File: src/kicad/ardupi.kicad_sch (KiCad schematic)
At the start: 60 parts, among them J1 Conn_01x02, J10 Conn_01x04, J11 TSW-108-08-L-T-RA, J2 Conn_01x10, J3 Conn_01x05, J4 Conn_01x04, J5 GPIO_CONNECTOR, J6 Conn_01x05, J7 Conn_01x06, J8 Conn_01x04, J9 Conn_01x02, U1 CAT24C256, U2 ULN2803ADW, U3 PCA9685BS, U4 ADS1115IRUGR, U5 MPU-9250, U6 BMP280

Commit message: fix layout
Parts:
- removed BT1: Battery, symbol Device:Battery
- removed C1: 100n, symbol Device:C_Small
- removed J1: Conn_01x02, Connector_JST:JST_EH_B2B-EH-A_1x02_P2.50mm_Vertical, symbol ardupi:Conn_01x02
- removed J5: GPIO_CONNECTOR, lib:PinSocket_2x20_P2.54mm_Vertical_Centered_Anchor, symbol Connector_Generic:Conn_02x20_Odd_Even
- removed JP1: ID_WP, symbol Jumper:SolderJumper_2_Open
- removed R1, R2: 3.9k, symbol Device:R_Small
- added C9: 100n, symbol Device:C_Small
- added J1: GPIO, Connector_PinSocket_2.54mm:PinSocket_2x20_P2.54mm_Vertical, symbol Connector_Generic:Conn_02x20_Odd_Even
- added JP2: ID_WP, symbol Jumper:SolderJumper_2_Open
- added R21, R22: 3.9k, symbol Device:R_Small
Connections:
- net +3V3: now also U1.8 (VCC), C9.2, J1.1 (Pin_1), J1.17 (Pin_17), JP2.2 (B), R21.2, R22.1
- net +5V: now also J1.2 (Pin_2), J1.4 (Pin_4)
- net BUZZER: now also J1.32 (Pin_32)
- net GND: now also U1.4 (VSS), C9.1, J1.14 (Pin_14), J1.20 (Pin_20), J1.25 (Pin_25), J1.30 (Pin_30), J1.34 (Pin_34), J1.39 (Pin_39), J1.6 (Pin_6), J1.9 (Pin_9)
- net GPIO14_TXD0: now also J1.8 (Pin_8)
- net GPIO15_RXD0: now also J1.10 (Pin_10)
- net GPIO18_GEN1: now also J1.12 (Pin_12)
- net GPIO23: now also J1.16 (Pin_16)
- net GPIO24: now also J1.18 (Pin_18)
- net GPIO25_GEN6: now also J1.22 (Pin_22)
- net ID_SCL: now also U1.6 (SCL), U1.7 (WP), J1.28 (Pin_28), JP2.1 (A), R22.2
- net ID_SDA: now also U1.5 (SDA), J1.27 (Pin_27), R21.1
- net LED1: now also J1.13 (Pin_13)
- net LED2: now also J1.15 (Pin_15)
- net LED3: now also J1.7 (Pin_7)
- net RC1: now also J1.29 (Pin_29)
- net RC2: now also J1.31 (Pin_31)
- net RC3: now also J1.33 (Pin_33)
- net RC4: now also J1.35 (Pin_35)
- net RC5: now also J1.37 (Pin_37)
- net RC6: now also J1.40 (Pin_40)
- net RC7: now also J1.38 (Pin_38)
- net RC8: now also J1.36 (Pin_36)
- net SCL1: now also J1.5 (Pin_5)
- net SDA1: now also J1.3 (Pin_3)
- net SPI_CE0_N: now also J1.24 (Pin_24)
- net SPI_CE1_N: now also J1.26 (Pin_26)
- net SPI_MISO: now also J1.21 (Pin_21)
- net SPI_MOSI: now also J1.19 (Pin_19)
- net SPI_SCLK: now also J1.23 (Pin_23)
- net SRVO_EN: now also J1.11 (Pin_11)
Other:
- title: ArduPi -> (none)
- moved on the sheet: C_PCA1, J11, R3, R4, R5, U1, U3

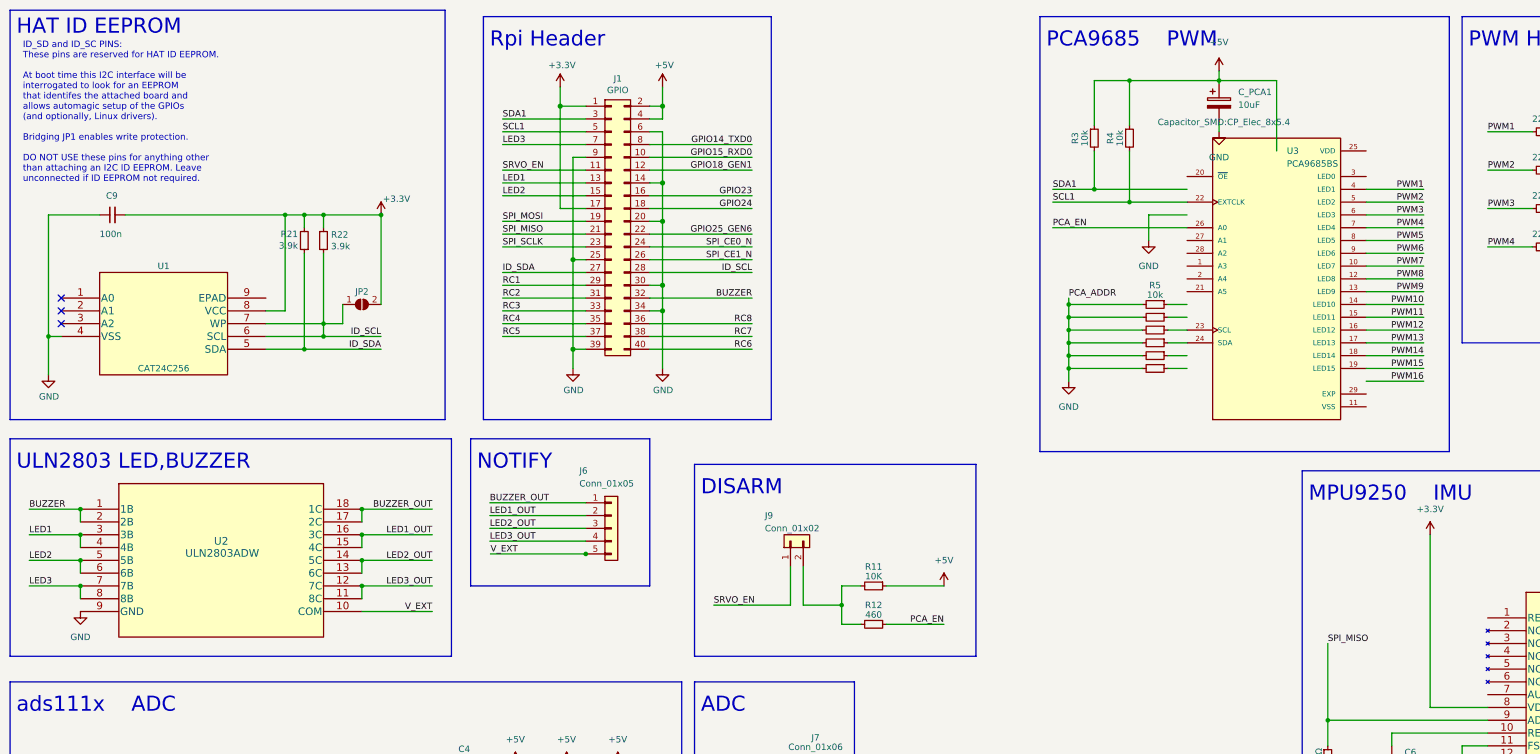
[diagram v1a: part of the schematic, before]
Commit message: replaced pca9685bs back to pca9685PW.
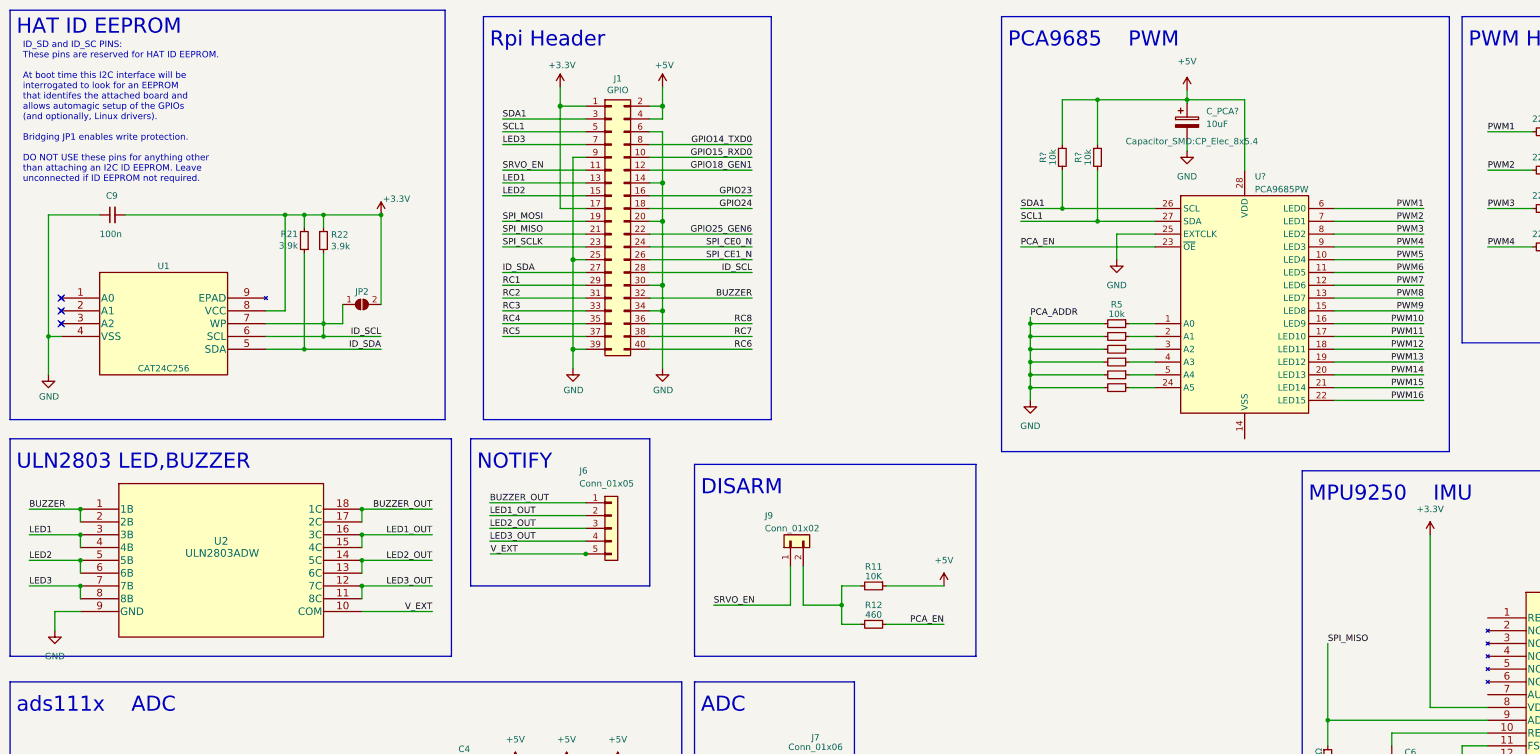
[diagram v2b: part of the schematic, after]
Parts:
- removed C_PCA1: 10uF, Capacitor_SMD:CP_Elec_8x5.4, symbol Device:C_Polarized
- removed R3, R4: 10k, Resistor_SMD:R_0402_1005Metric, symbol Device:R_Small
- removed U3: PCA9685BS, Ardupi:PCA9685BS_118, symbol ardupi:PCA9685BS,118
- added C_PCA?: 10uF, Capacitor_SMD:CP_Elec_8x5.4, symbol Device:C_Polarized
- added R? (x2): 10k, Resistor_SMD:R_0402_1005Metric, symbol Device:R_Small
- added U?: PCA9685PW, Package_SO:TSSOP-28_4.4x9.7mm_P0.65mm, symbol Driver_LED:PCA9685PW
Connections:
- net +5V: now also C_PCA?.1, R?.1, R?.1, U?.28 (VDD)
- net GND: now also C_PCA?.2, U?.25 (EXTCLK)
- net PCA_EN: now also U?.23 (~{OE})
- net PWM1: now also U?.6 (LED0)
- net PWM10: now also U?.16 (LED9)
- net PWM11: now also U?.17 (LED10)
- net PWM12: now also U?.18 (LED11)
- net PWM13: now also U?.19 (LED12)
- net PWM14: now also U?.20 (LED13)
- net PWM15: now also U?.21 (LED14)
- net PWM16: now also U?.22 (LED15)
- net PWM2: now also U?.7 (LED1)
- net PWM3: now also U?.8 (LED2)
- net PWM4: now also U?.9 (LED3)
- net PWM5: now also U?.10 (LED4)
- net PWM6: now also U?.11 (LED5)
- net PWM7: now also U?.12 (LED6)
- net PWM8: now also U?.13 (LED7)
- net PWM9: now also U?.15 (LED8)
- net SCL1: now also R?.2, U?.27 (SDA)
- net SDA1: now also R?.2, U?.26 (SCL)
- net at R7.1: now also U?.3 (A2)
- net at R6.1: now also U?.2 (A1)
- net at R8.1: now also U?.4 (A3)
- net at R5.1: now also U?.1 (A0)
- net at R10.1: now also U?.24 (A5)
- net at R9.1: now also U?.5 (A4)
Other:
- moved on the sheet: R5

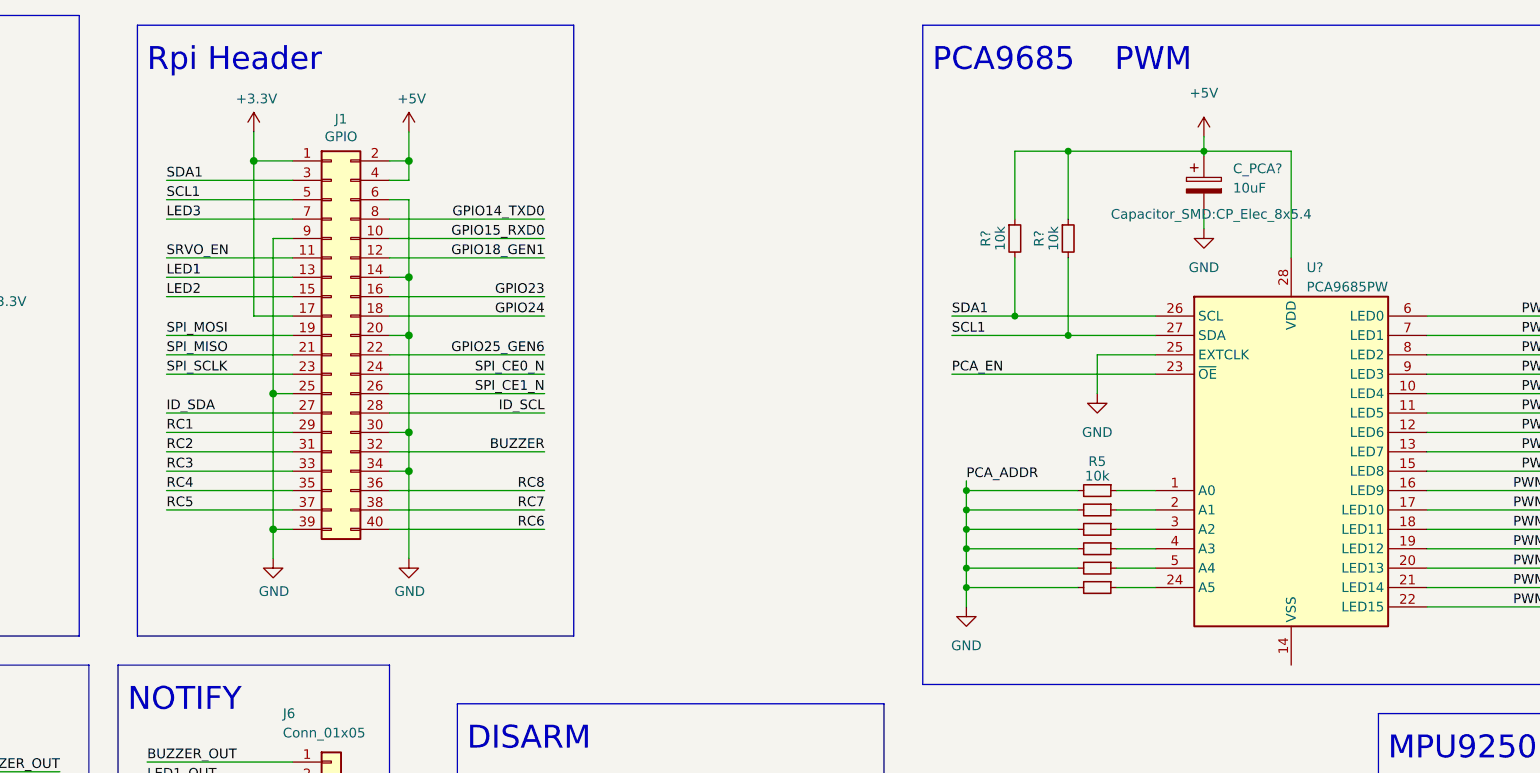
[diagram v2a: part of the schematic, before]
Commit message: pca9685bs -> pca9685PW
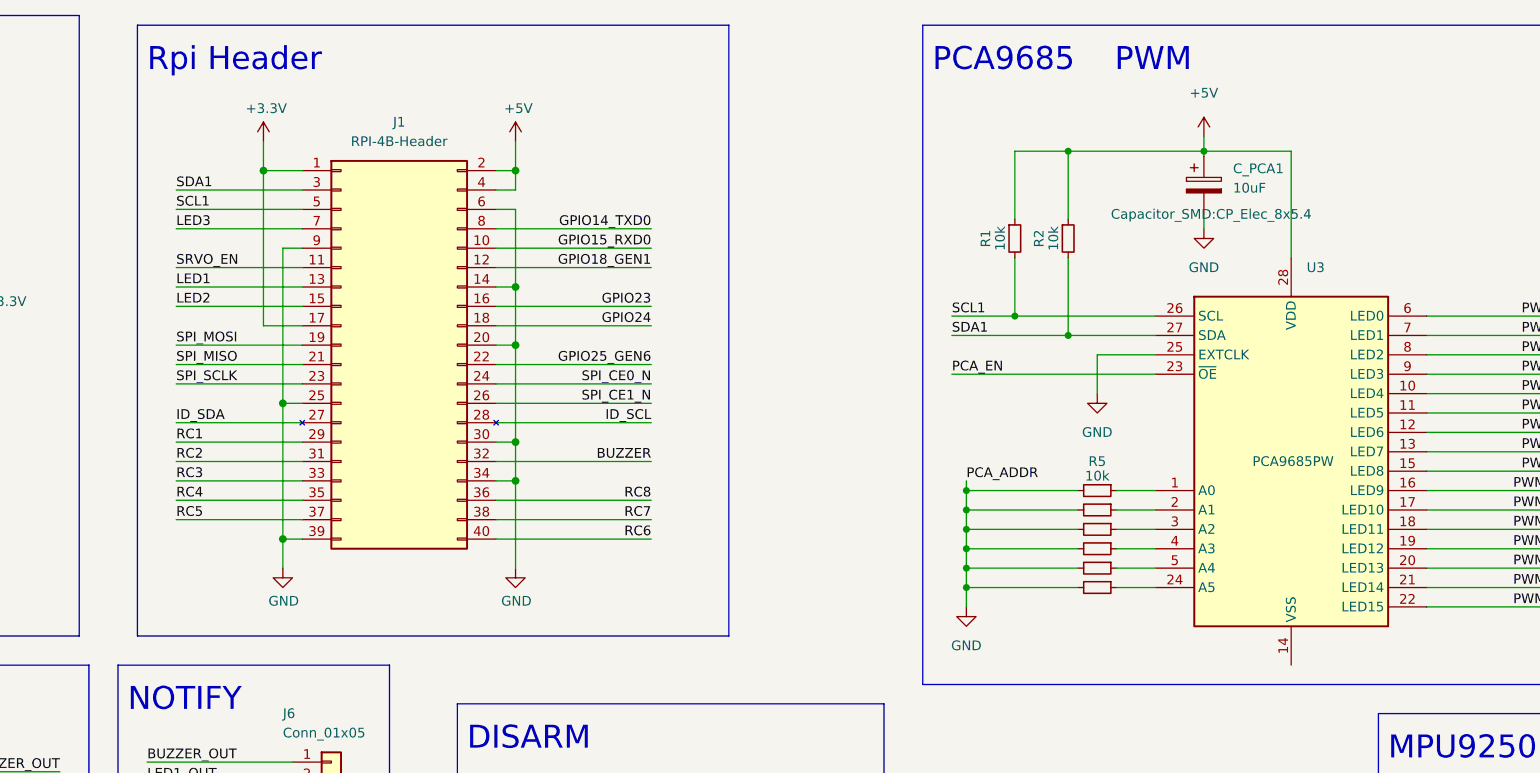
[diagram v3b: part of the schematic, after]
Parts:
- removed J1: GPIO, Connector_PinSocket_2.54mm:PinSocket_2x20_P2.54mm_Vertical, symbol Connector_Generic:Conn_02x20_Odd_Even
- added J1: RPI-4B-Header, Connector_PinSocket_2.54mm:PinSocket_2x20_P2.54mm_Vertical, symbol ArduPi:RPI-4B-Header
- gave numbers to parts that had none: 4
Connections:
- net +3V3: now also J1.1 (+3.3V), J1.17 (+3.3V)
- net +5V: now also J1.2 (+5V), J1.4 (+5V)
- net BUZZER: now also J1.32 (GPIO12)
- net GND: now also J1.14 (GND), J1.20 (GND), J1.25 (GND), J1.30 (GND), J1.34 (GND), J1.39 (GND), J1.6 (GND), J1.9 (GND)
- net GPIO14_TXD0: now also J1.8 (UART0_TX)
- net GPIO15_RXD0: now also J1.10 (UART0_RX)
- net GPIO18_GEN1: now also J1.12 (GPIO18)
- net GPIO23: now also J1.16 (GPIO23)
- net GPIO24: now also J1.18 (GPIO24)
- net GPIO25_GEN6: now also J1.22 (GPIO25)
- net ID_SCL: now also J1.28 (Reserved)
- net ID_SDA: now also J1.27 (Reserved)
- net LED1: now also J1.13 (GPIO27)
- net LED2: now also J1.15 (GPIO22)
- net LED3: now also J1.7 (GPIO4)
- net RC1: now also J1.29 (GPIO5)
- net RC2: now also J1.31 (GPIO6)
- net RC3: now also J1.33 (GPIO13)
- net RC4: now also J1.35 (GPIO_19)
- net RC5: now also J1.37 (GPIO26)
- net RC6: now also J1.40 (GPIO21)
- net RC7: now also J1.38 (GPIO20)
- net RC8: now also J1.36 (GPIO16)
- net SCL1: now also R1.2, U3.26 (SCL), J1.5 (GPIO3); no longer R2.2, U3.27 (SDA)
- net SDA1: now also R2.2, U3.27 (SDA), J1.3 (GPIO2); no longer R1.2, U3.26 (SCL)
- net SPI_CE0_N: now also J1.24 (GPIO8)
- net SPI_CE1_N: now also J1.26 (GPIO7)
- net SPI_MISO: now also J1.21 (GPIO9)
- net SPI_MOSI: now also J1.19 (GPIO10)
- net SPI_SCLK: now also J1.23 (GPIO11)
- net SRVO_EN: now also J1.11 (GPIO17)

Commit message: version bump
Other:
- title: (none) -> ArduPi
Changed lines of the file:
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@@
   (paper "A3")
   (title_block
-    (date "15 nov 2012")
+    (title "ArduPi")
+    (date "2022-06-05")
+    (rev "0.1.4")
+    (comment 1 "Author: Muhammad Hefny")
+    (comment 2 "Author: Shaun Lloyd")
   )
   (junction (at 325.12 66.04) (diameter 0) (color 0 0 0 0)

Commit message: elec: PCA9685 jumpers
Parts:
- added JP? (x6): ID_WP, symbol Jumper:SolderJumper_2_Open
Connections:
- net +5V: now also JP?.1 (A), JP?.1 (A), JP?.1 (A), JP?.1 (A), JP?.1 (A), JP?.1 (A)
- net at R7.1, U3.3 (A2): now also JP?.2 (B)
- net at R6.1, U3.2 (A1): now also JP?.2 (B)
- net at R5.1, U3.1 (A0): now also JP?.2 (B)
- net at R10.1, U3.24 (A5): now also JP?.2 (B)
- net at R8.1, U3.4 (A3): now also JP?.2 (B)
- net at R9.1, U3.5 (A4): now also JP?.2 (B)
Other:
- moved on the sheet: R5

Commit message: +ADS1115IDGSR update all symbol footprints VSS = GND
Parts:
- removed JP? (x6): ID_WP, symbol Jumper:SolderJumper_2_Open
- removed U4: ADS1115IRUGR, Ardupi:ADS1115IRUGT, symbol ardupi:ADS1115IRUGT
- added SJ_A1, SJ_A2, SJ_A3, SJ_A4, SJ_A5, SJ_A6: SOLDERJUMPERREFLOW_NOPASTE, Ardupi:SOLDERJUMPER_REFLOW_NOPASTE, symbol ArduPi:SOLDERJUMPERREFLOW_NOPASTE
- added U4: ADS1115IDGSR, Ardupi:ADS1115IDGSR, symbol ArduPi:ADS1115IDGSR
- C9: footprint (none) -> Capacitor_Tantalum_SMD:CP_EIA-1608-10_AVX-L
- JP2: footprint (none) -> Ardupi:SOLDERJUMPER_REFLOW_NOPASTE
- R21, R22: footprint (none) -> Resistor_SMD:R_0402_1005Metric
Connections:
- net +5V: now also R32.1, SJ_A1.1, SJ_A2.1, SJ_A3.1, SJ_A4.1, SJ_A5.1, SJ_A6.1, U4.8 (VDD); no longer R32.2
- net AIO0: now also U4.4 (AIN0)
- net AIO1: now also U4.5 (AIN1)
- net AIO2: now also U4.10 (SCL)
- net AIO3: now also U4.9 (SDA)
- net GND: now also U3.14 (VSS), U5.18 (GND), U4.3 (GND)
- net SCL1: now also U4.6 (AIN2)
- net SDA1: now also R32.2, U4.7 (AIN3); no longer R32.1
- net at R7.1, U3.3 (A2): now also SJ_A3.2
- net at R27.1: now also U4.1 (ADDR)
- net at R9.1, U3.5 (A4): now also SJ_A5.2
- net at R10.1, U3.24 (A5): now also SJ_A6.2
- net at R6.1, U3.2 (A1): now also SJ_A2.2
- net at R5.1, U3.1 (A0): now also SJ_A1.2
- net at R8.1, U3.4 (A3): now also SJ_A4.2
- net at R25.1: now also U4.2 (ALERT_RDY)
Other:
- note added: "ADS1115IDGSR ADC"
- note removed: "ads111x ADC"
- moved on the sheet: C2, C3, C4, C5, C6, C7, C8, C9, C_PCA1, J1, J10, J11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

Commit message: update symbol definitions, all correct with exception noted in issues
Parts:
- removed U1: CAT24C256, Ardupi:CAT24C256HU4IGT3, symbol ardupi:CAT24C256HU4IGT3
- removed U2: ULN2803ADW, Ardupi:ULN2803ADWR, symbol ardupi:ULN2803ADWR
- removed U3: PCA9685PW, Package_SO:TSSOP-28_4.4x9.7mm_P0.65mm, symbol Driver_LED:PCA9685PW
- removed U6: BMP280, Ardupi:bmp280, symbol ardupi:BMP280
- added U1: CAT24C256HU4IGT3, Ardupi:CAT24C256HU4IGT3, symbol ArduPi:CAT24C256HU4IGT3
- added U2: ULN2803ADWR, Ardupi:ULN2803ADWR, symbol ArduPi:ULN2803ADWR
- added U3: PCA9685PW, Ardupi:PCA9685PW_118, symbol ArduPi:PCA9685PW
- added U6: BMP280, Ardupi:bmp280, symbol ArduPi:BMP280
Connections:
- net +3V3: now also U1.8 (VCC), U6.6 (VDDIO), U6.8 (VDD); no longer J1.1 (+3.3V), J1.17 (+3.3V)
- net +5V: now also U3.28 (VDD)
- net BUZZER: now also U2.1 (1B), U2.2 (2B)
- net BUZZER_OUT: now also U2.17 (2C), U2.18 (1C)
- net GND: now also U1.4 (VSS), U2.9 (GND), U3.14 (VSS), U3.25 (EXTCLK), U6.1 (GND), U6.7 (GND); no longer J1.25 (GND), J1.39 (GND), J1.9 (GND)
- net ID_SCL: now also U1.6 (SCL), U1.7 (WP)
- net ID_SDA: now also U1.5 (SDA); no longer J1.27 (Reserved)
- net LED1: now also U2.3 (3B), U2.4 (4B); no longer J1.13 (GPIO27)
- net LED1_OUT: now also U2.15 (4C), U2.16 (3C)
- net LED2: now also U2.5 (5B), U2.6 (6B); no longer J1.15 (GPIO22)
- net LED2_OUT: now also U2.13 (6C), U2.14 (5C)
- net LED3: now also U2.7 (7B), U2.8 (8B); no longer J1.7 (GPIO4)
- net LED3_OUT: now also U2.11 (8C), U2.12 (7C)
- net PCA_EN: now also U3.23 (~{OE})
- net PWM1: now also U3.6 (LED0)
- net PWM10: now also U3.16 (LED9)
- net PWM11: now also U3.17 (LED10)
- net PWM12: now also U3.18 (LED11)
- net PWM13: now also U3.19 (LED12)
- net PWM14: now also U3.20 (LED13)
- net PWM15: now also U3.21 (LED14)
- net PWM16: now also U3.22 (LED15)
- net PWM2: now also U3.7 (LED1)
- net PWM3: now also U3.8 (LED2)
- net PWM4: now also U3.9 (LED3)
- net PWM5: now also U3.10 (LED4)
- net PWM6: now also U3.11 (LED5)
- net PWM7: now also U3.12 (LED6)
- net PWM8: now also U3.13 (LED7)
- net PWM9: now also U3.15 (LED8)
- net RC1: no longer J1.29 (GPIO5)
- net RC2: no longer J1.31 (GPIO6)
- net RC3: no longer J1.33 (GPIO13)
- net RC4: no longer J1.35 (GPIO_19)
- net RC5: no longer J1.37 (GPIO26)
- net SCL1: now also U3.26 (SCL); no longer J1.5 (GPIO3)
- net SDA1: now also U3.27 (SDA); no longer J1.3 (GPIO2)
- net SPI_CE1_N: now also U6.2 (CSB)
- net SPI_MISO: now also U6.5 (SDO); no longer J1.21 (GPIO9)
- net SPI_MOSI: now also U6.3 (SDI); no longer J1.19 (GPIO10)
- net SPI_SCLK: now also U6.4 (SCK); no longer J1.23 (GPIO11)
- net SRVO_EN: no longer J1.11 (GPIO17)
- net V_EXT: now also U2.10 (COM)
- net at R7.1, SJ_A3.2: now also U3.3 (A2)
- net at R8.1, SJ_A4.2: now also U3.4 (A3)
- net at R10.1, SJ_A6.2: now also U3.24 (A5)
- net at R6.1, SJ_A2.2: now also U3.2 (A1)
- net at R5.1, SJ_A1.2: now also U3.1 (A0)
- net at R9.1, SJ_A5.2: now also U3.5 (A4)
- no-connect marks 3 -> 0
